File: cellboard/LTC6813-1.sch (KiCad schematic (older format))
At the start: 36 parts, among them CN1 10nF_array, CN2 10nF_array, CN3 10nF_array, CN4 10nF_array, CN5 10nF_array, J19 CONN_1X02, J20 CONN_1X02, U1 LTC6813-1, U3 HM2103, U4 HM2103

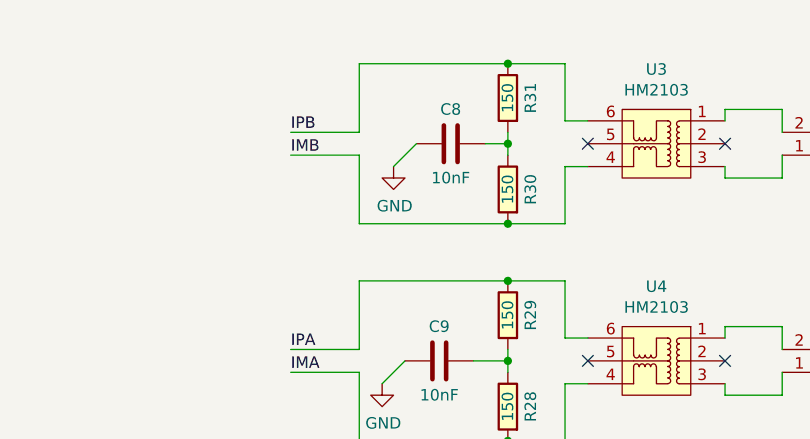
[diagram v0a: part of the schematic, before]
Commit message: removed rescue references and rescue library
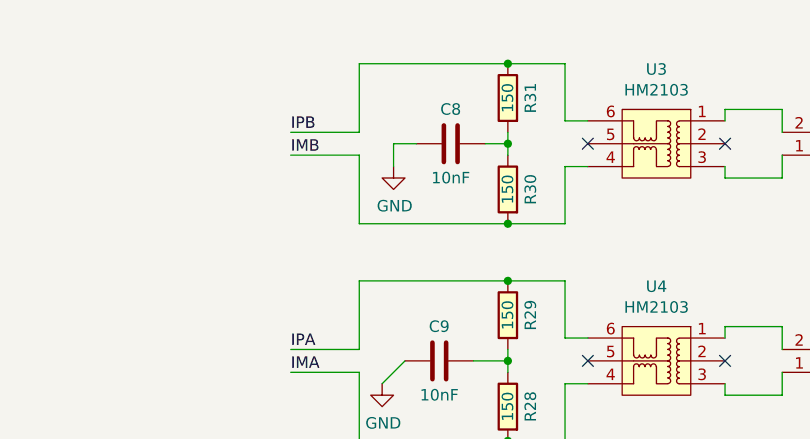
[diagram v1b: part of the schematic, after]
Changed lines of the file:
@@
 $EndComp
 Wire Wire Line
-	8750 1150 8850 1050
+	8750 1050 8850 1050
 $Comp
 L CellsBoard:GND #PWR0111
@@
 Wire Wire Line
 	4500 5000 4500 5050
+Wire Wire Line
+	8750 1050 8750 1150
 $EndSCHEMATC
